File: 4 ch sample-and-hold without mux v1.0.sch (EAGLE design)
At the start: 25 parts, among them IC5 TL074D

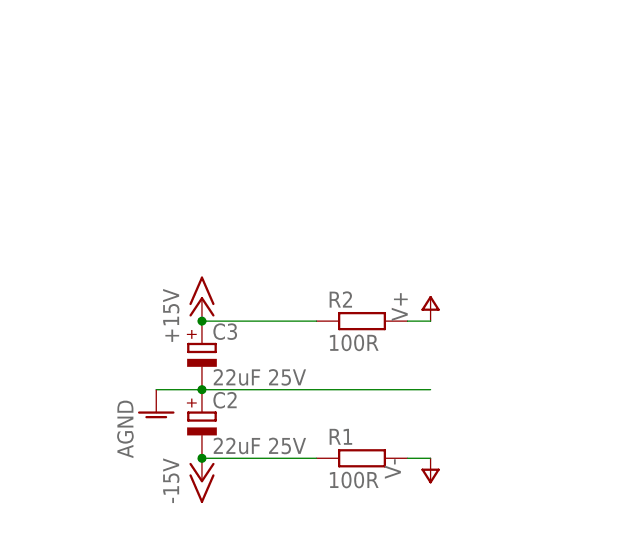
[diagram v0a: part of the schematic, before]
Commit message: Just missing logo
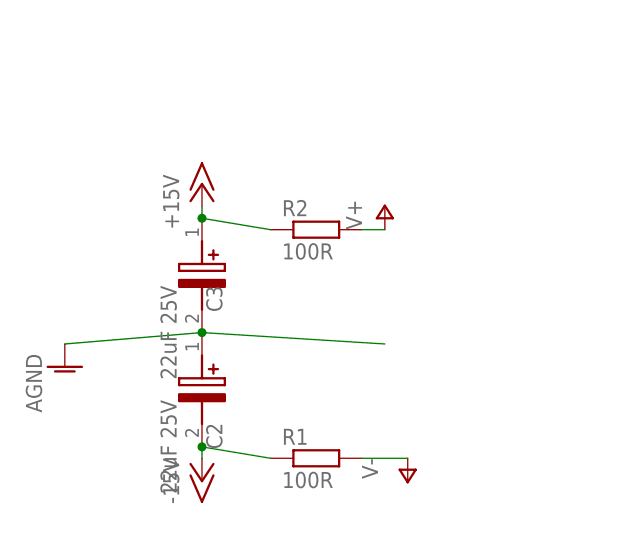
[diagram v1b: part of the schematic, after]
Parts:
- C2, C3: device resistor:CPOL-EUE2.5-5 -> joakim-jclpcb:VZL101M1CTR-0606
- SV1, SV2: device con-lstb:MA04-1 -> joakim:MA04-1JP
- SV3: device con-lstb:MA03-1 -> joakim:MA03-1JP
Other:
- moved on the sheet: R1, R2

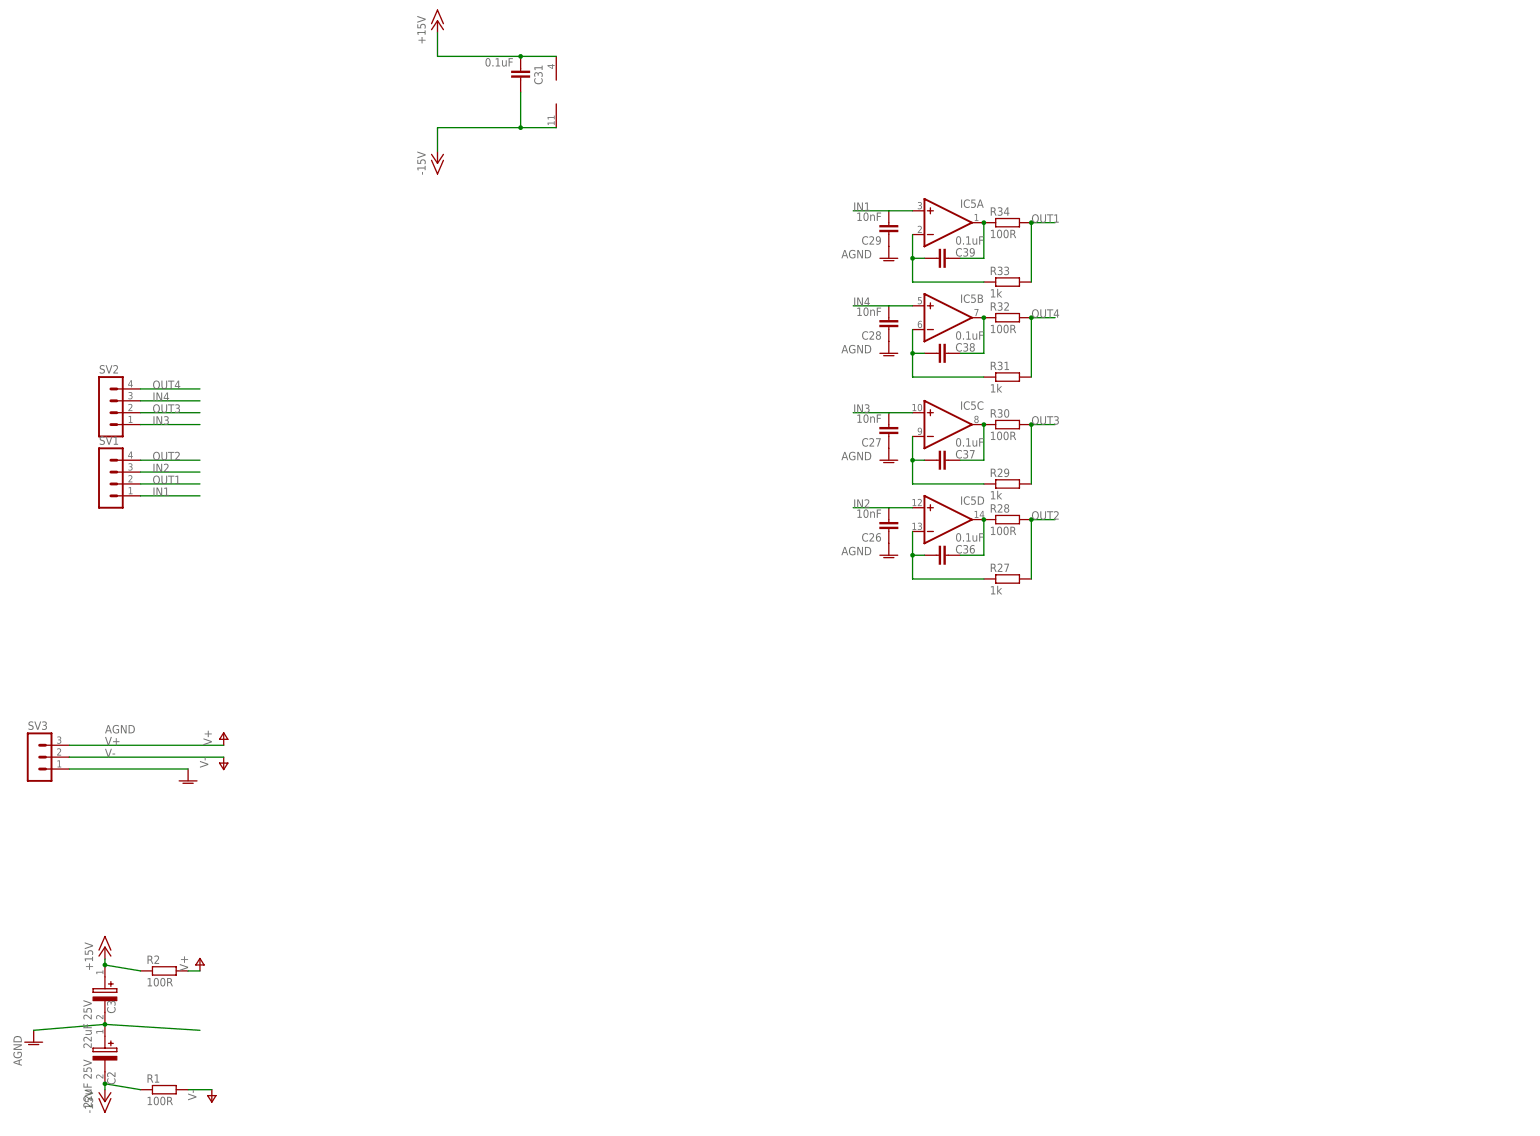
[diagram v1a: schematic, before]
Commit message: Created parts list, cleaned up schematics
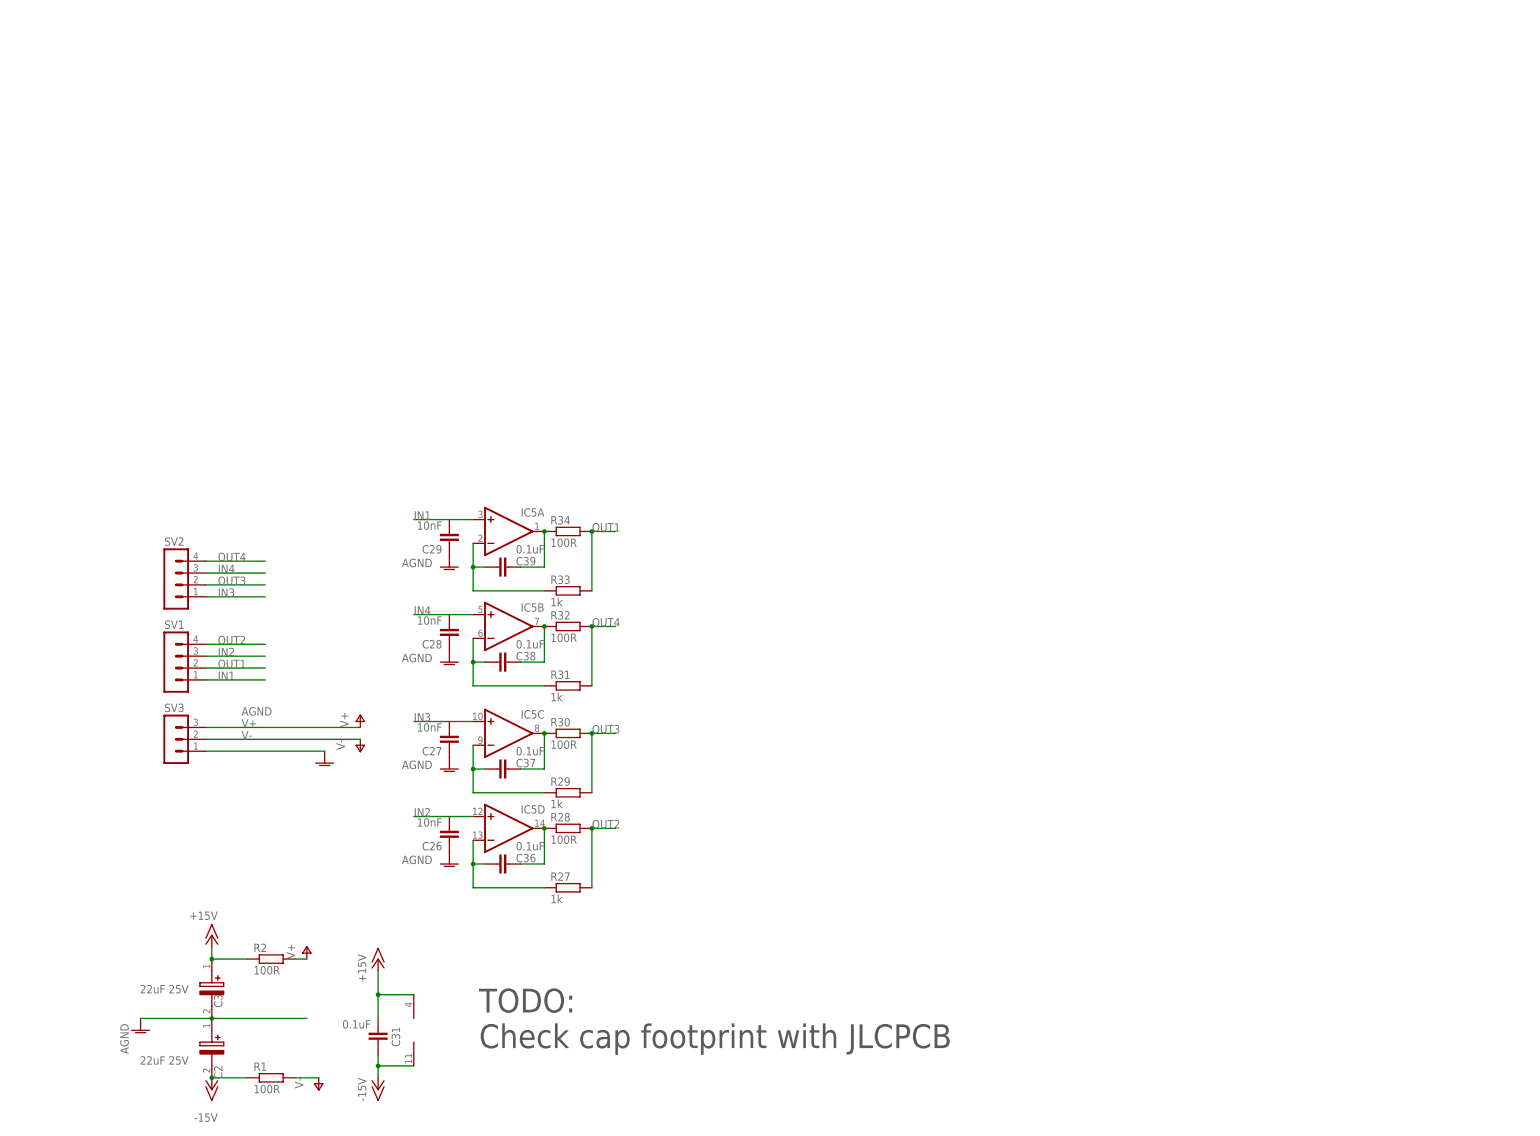
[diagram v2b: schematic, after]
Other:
- note added: "TODO: Check cap footprint with JLCPCB"
- moved on the sheet: C2, C26, C27, C28, C29, C3, C31, C36, C37, C38, C39, IC5A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

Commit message: Added bom and gerber
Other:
- note added: "with 0-10V input: Max current through resistors when feeding into a 10k res is: 100R: 1mA = 0.1mW 1k: 63nA OK with 1/10w resistors"
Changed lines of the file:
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@@
 <setting verticaltext="up"/>
 </settings>
-<grid distance="0.05" unitdist="inch" unit="inch" style="lines" multiple="1" display="no" altdistance="0.01" altunitdist="inch" altunit="inch"/>
+<grid distance="0.1" unitdist="inch" unit="inch" style="lines" multiple="1" display="no" altdistance="0.01" altunitdist="inch" altunit="inch"/>
 <layers>
 <layer number="1" name="Top" color="4" fill="1" visible="no" active="no"/>
@@
 <text x="26.67" y="-77.47" size="5.08" layer="97">TODO:
 Check cap footprint with JLCPCB</text>
+<text x="101.6" y="7.62" size="5.08" layer="97">with 0-10V input:
+Max current through resistors when
+feeding into a 10k res is:
+100R: 1mA = 0.1mW
+1k: 63nA
+OK with 1/10w resistors</text>
 </plain>
 <instances>

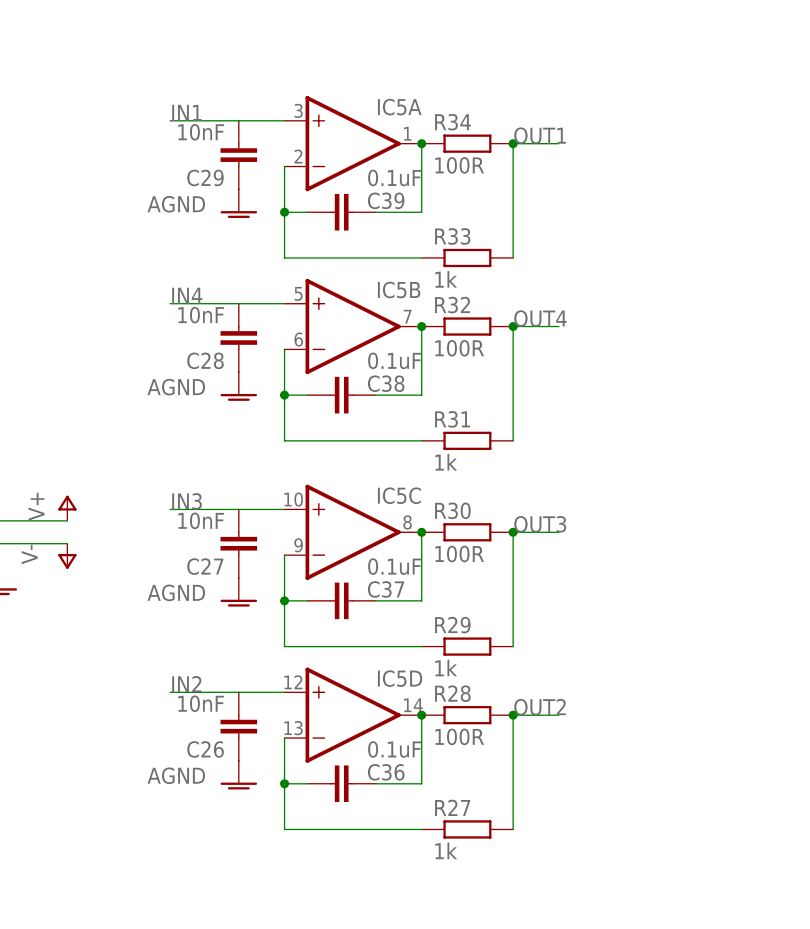
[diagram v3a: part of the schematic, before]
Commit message: changed from 0.1uF to 330pF to align with Fat Controller circuit
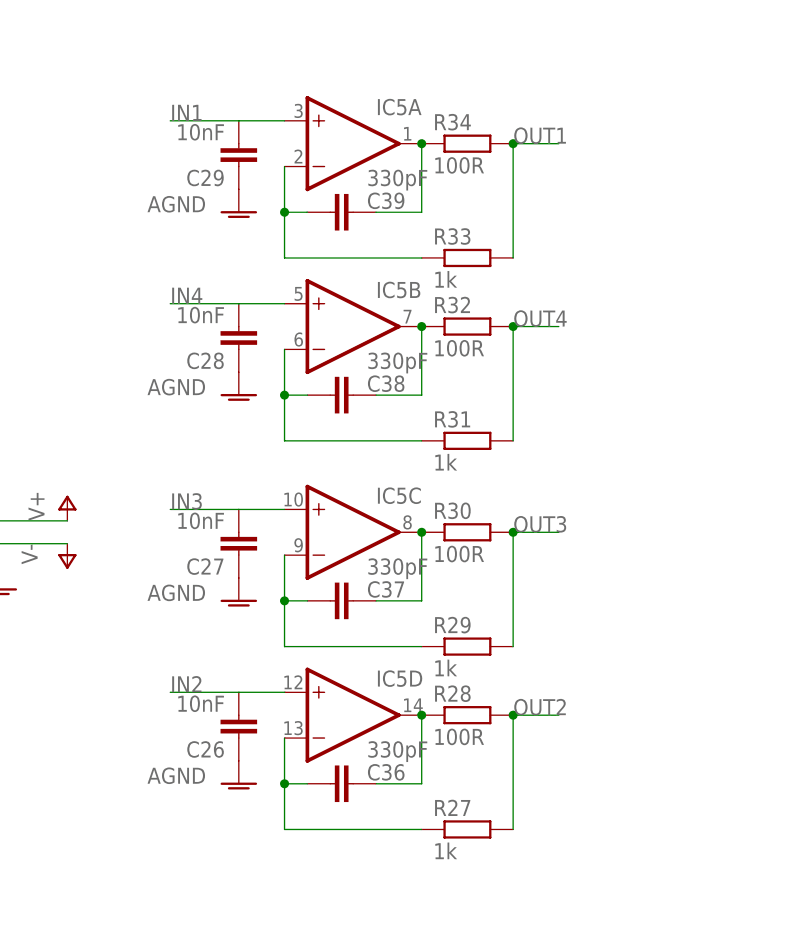
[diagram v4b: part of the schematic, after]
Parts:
- C36, C37, C38, C39: value 0.1uF -> 330pF
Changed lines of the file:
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@@
 <part name="AGND19" library="supply1" deviceset="AGND" device=""/>
 <part name="AGND20" library="supply1" deviceset="AGND" device=""/>
-<part name="C39" library="resistor" deviceset="C-EU" device="C0603" value="0.1uF"/>
+<part name="C39" library="resistor" deviceset="C-EU" device="C0603" value="330pF"/>
 <part name="R34" library="resistor" deviceset="R-EU_" device="R0603" value="100R"/>
 <part name="R33" library="resistor" deviceset="R-EU_" device="R0603" value="1k"/>
 <part name="R32" library="resistor" deviceset="R-EU_" device="R0603" value="100R"/>
 <part name="R31" library="resistor" deviceset="R-EU_" device="R0603" value="1k"/>
-<part name="C38" library="resistor" deviceset="C-EU" device="C0603" value="0.1uF"/>
-<part name="C37" library="resistor" deviceset="C-EU" device="C0603" value="0.1uF"/>
+<part name="C38" library="resistor" deviceset="C-EU" device="C0603" value="330pF"/>
+<part name="C37" library="resistor" deviceset="C-EU" device="C0603" value="330pF"/>
 <part name="R30" library="resistor" deviceset="R-EU_" device="R0603" value="100R"/>
 <part name="R29" library="resistor" deviceset="R-EU_" device="R0603" value="1k"/>
-<part name="C36" library="resistor" deviceset="C-EU" device="C0603" value="0.1uF"/>
+<part name="C36" library="resistor" deviceset="C-EU" device="C0603" value="330pF"/>
 <part name="R27" library="resistor" deviceset="R-EU_" device="R0603" value="1k"/>
 <part name="R28" library="resistor" deviceset="R-EU_" device="R0603" value="100R"/>
